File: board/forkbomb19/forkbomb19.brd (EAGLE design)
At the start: 89.2 x 57 mm, 67 parts, among them T3 MMUN2133LT1G, U1 ESP-WROOM-03, U4 TPS61090RSAR, U5 MCP73871, X3 POT_GND, X4 POT_3V3, X5 POT_SIG

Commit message: performing board review
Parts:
- TOUCH: value TOUCHPAD -> TOUCHPADTOUCH_BLANK; device forkbomb19:TOUCHPAD_9.5MM -> forkbomb19:TOUCH_BLANK
- moved LOGO1 147.7 mm to (118.5, 83.1), flipped to the bottom
- moved X3 80.8 mm to (157.1, 77.9)
- moved X5 80.8 mm to (156.8, 71.6)
- moved C14 80.6 mm to (121.3, 63.3)
- moved C9 80.6 mm to (83.6, 80.2)
- moved CHRG 80.6 mm to (88.9, 54.1)
- moved FID1 80.6 mm to (76.8, 35.8)
- moved FID3 80.6 mm to (159.3, 87.0)
- moved FID4 80.6 mm to (75.3, 70.1)
- moved LOGO_G 80.6 mm to (145.7, 39.1)
- moved LOW_BATT 80.6 mm to (91.0, 37.4)
- moved R11 80.6 mm to (150.3, 46.0)
- moved R12 80.6 mm to (85.5, 68.9)
- moved R18 80.6 mm to (80.4, 47.1)
- moved R19 80.6 mm to (85.6, 38.8)
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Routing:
- net TOUCH2: track 74.7 -> 72.1 mm
- net GND: vias 33 -> 34
- net N$23: vias 0 -> 2
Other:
- outline, holes or cut-outs redrawn
- board text added: "Grant Haack"
- board text added: "Open Source Hardware CC-BY-SA-4.0"
- board text added: "ghaack ichorous squar3r00t"

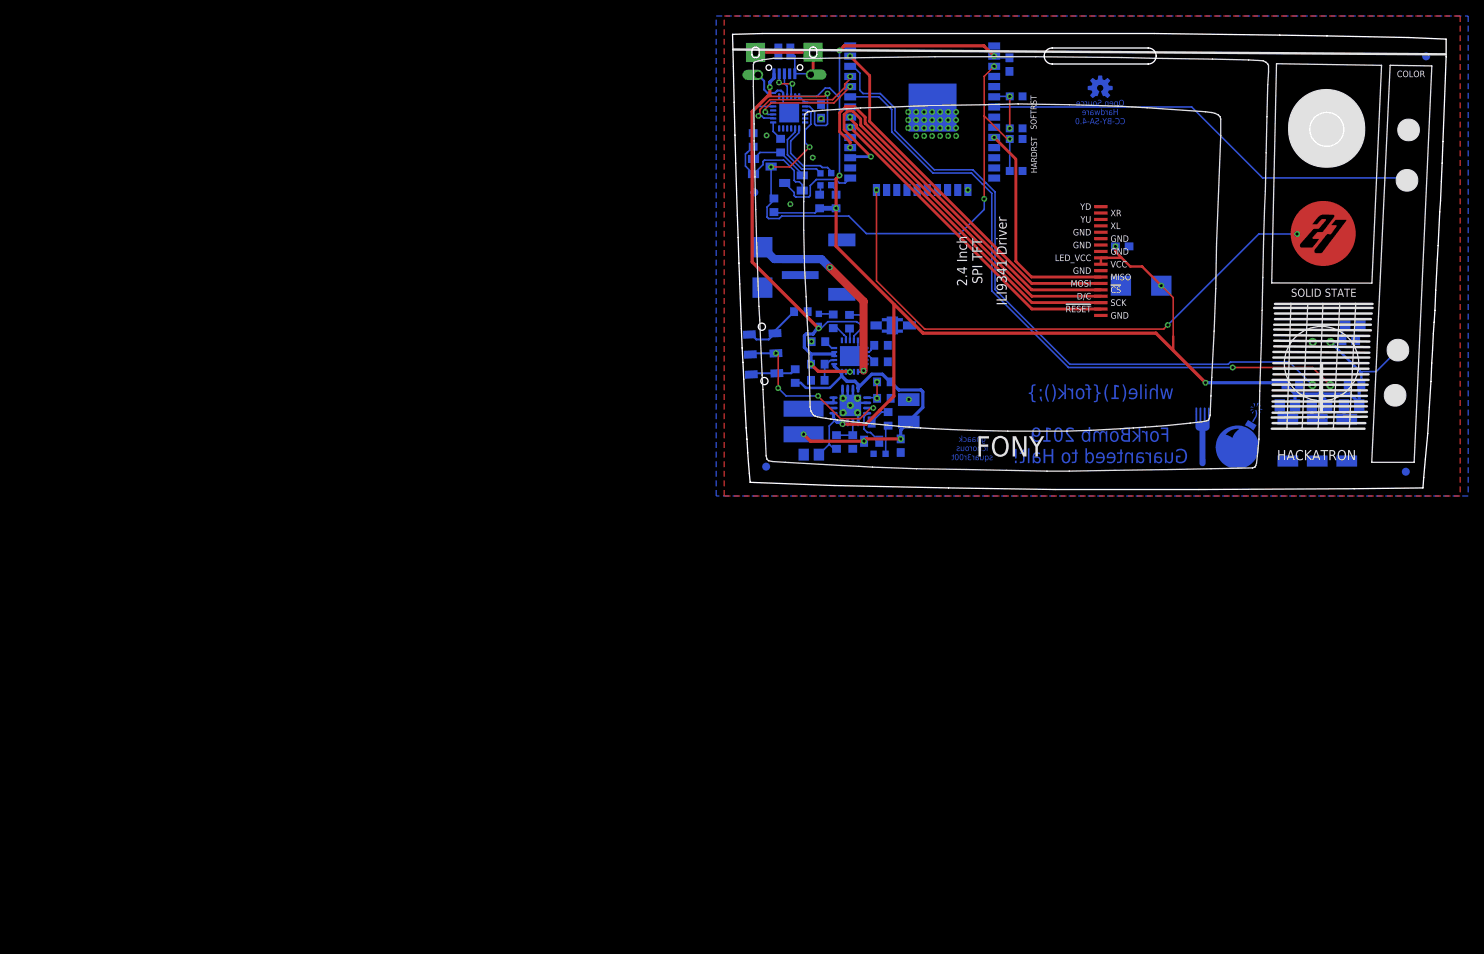
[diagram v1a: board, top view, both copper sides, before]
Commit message: TODO: Add rotary encoder, add another button, pwm the lights
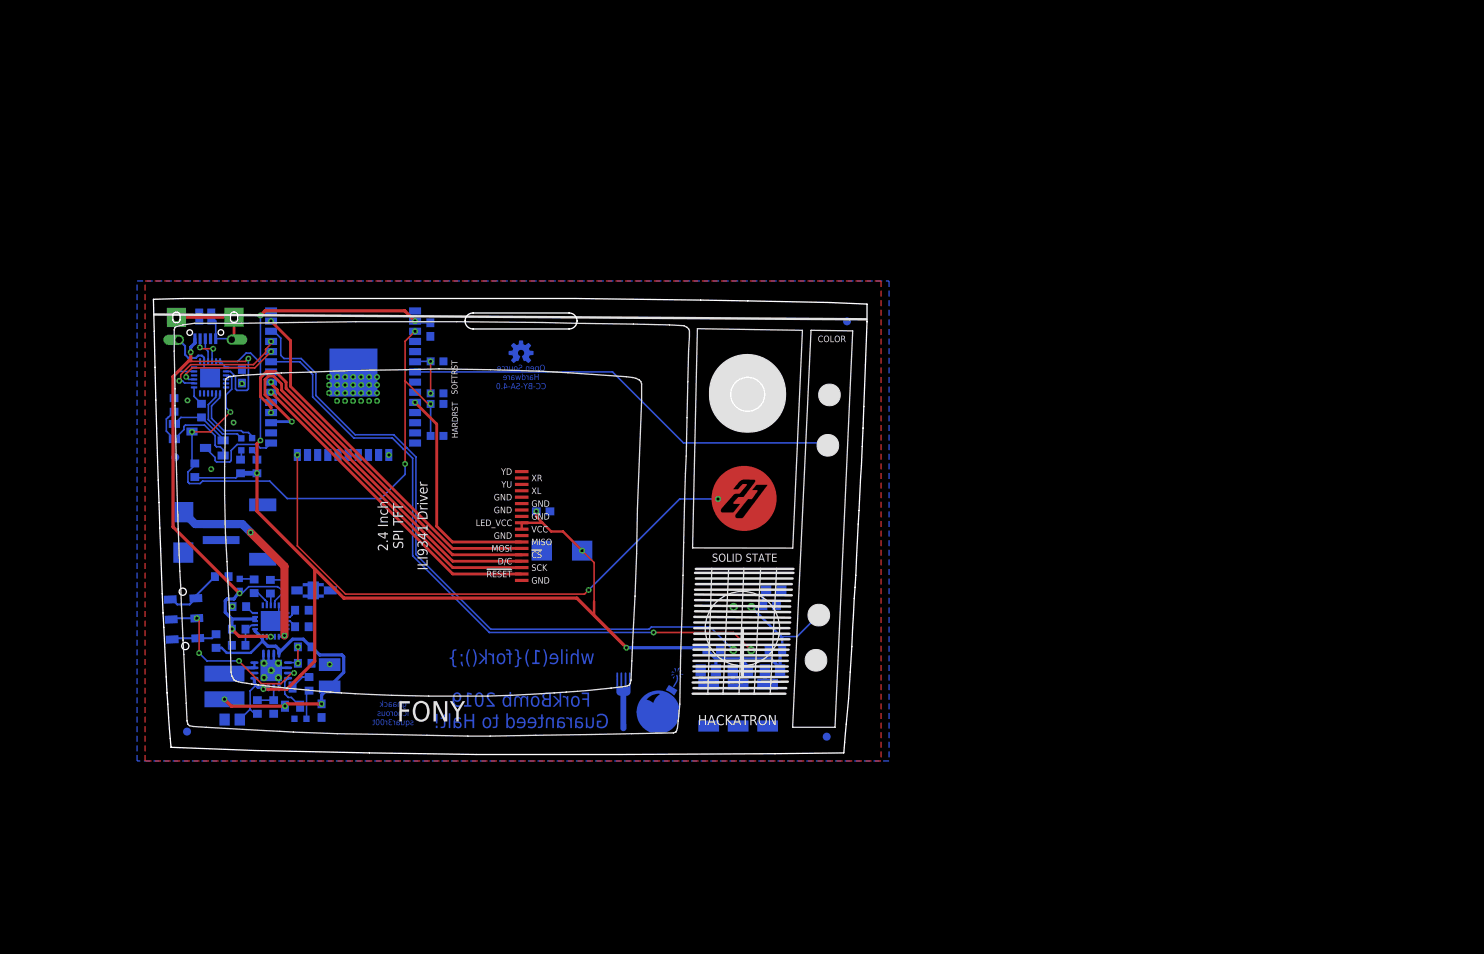
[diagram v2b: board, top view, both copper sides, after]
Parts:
- moved C1 79.6 mm to (34.8, 52.9)
- moved C14 79.6 mm to (48.9, 30.2)
- moved C9 79.6 mm to (11.3, 47.1)
- moved FID3 79.6 mm to (86.9, 53.9)
- moved LOGO_G 79.6 mm to (73.3, 5.94)
- moved R11 79.6 mm to (77.9, 12.9)
- moved R22 79.6 mm to (69.5, 10.3)
- moved R29 79.6 mm to (18.7, 15.8)
- moved R30 79.6 mm to (18.7, 17.8)
- moved R7 79.6 mm to (2.76, 43.5)
- moved U$7 79.6 mm to (73.8, 15.5)
- moved X3 79.6 mm to (84.7, 44.8)
- moved B1 79.6 mm to (12.3, 27.6)
- moved C10 79.6 mm to (3.92, 27.5)
- moved C11 79.6 mm to (77.2, 18.3)
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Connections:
- removed net TSCRN_X1: U1.13
- removed net TSCRN_X2: U1.14
- removed net TSCRN_Y1: U1.11
- removed net TSCRN_Y2: U1.12

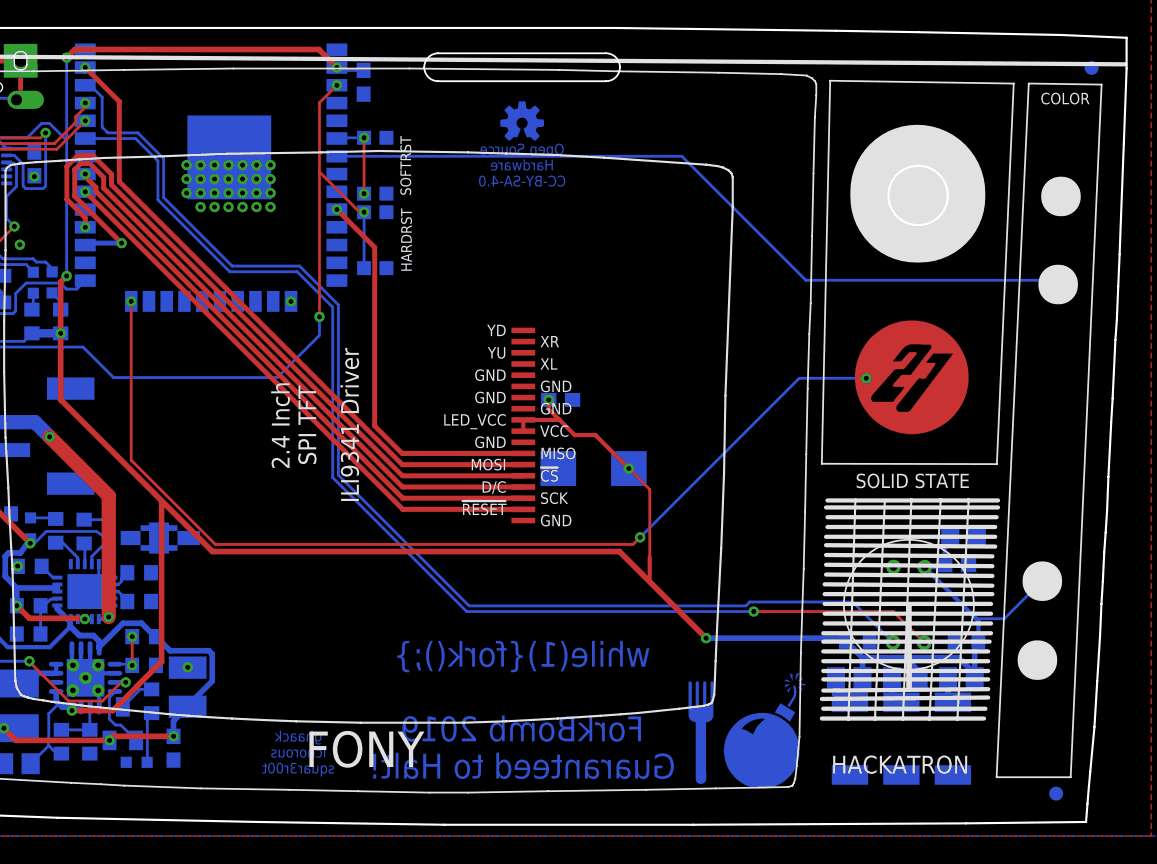
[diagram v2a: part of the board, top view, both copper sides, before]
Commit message: added PWM control for LEDs, swapped the potentiometer for a rotary encoder, and added a menu button
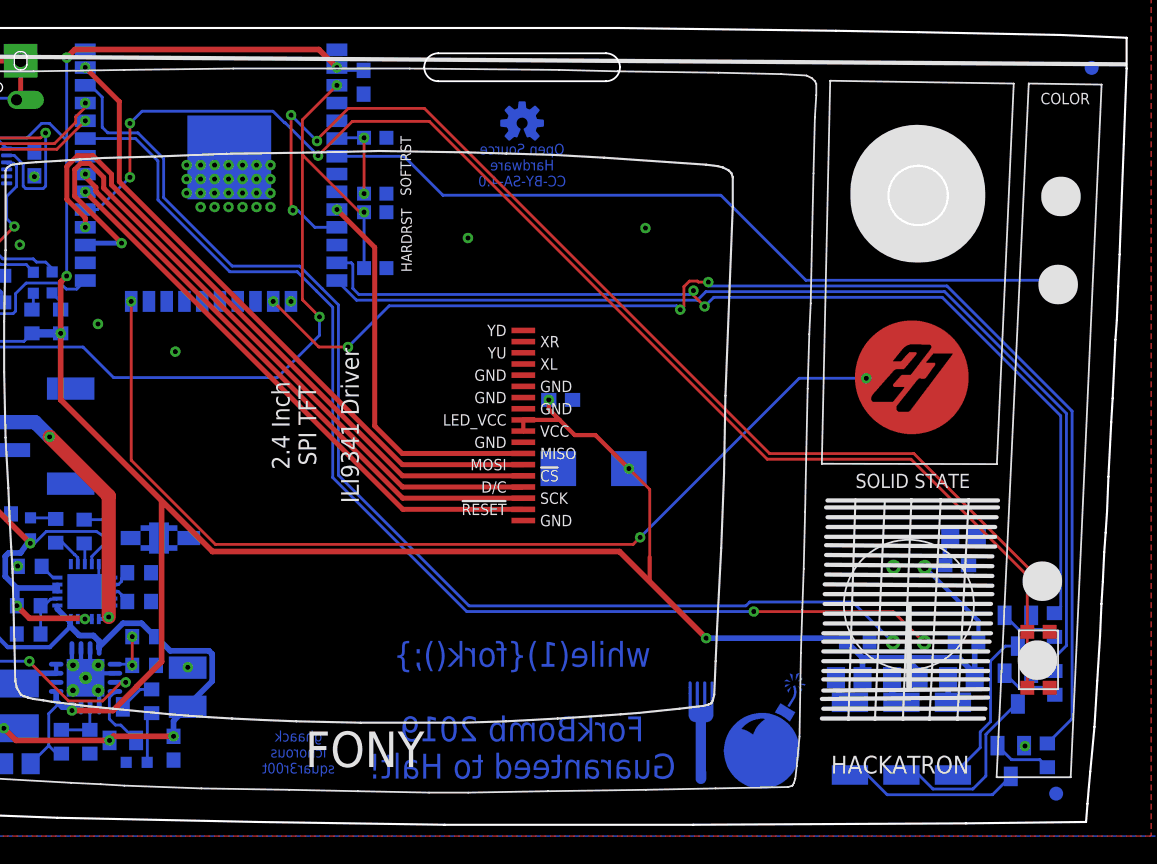
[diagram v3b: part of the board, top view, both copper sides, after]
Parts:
- added MENU: (no value), adafruit:KMR2
- added R13, R4, R5: 1K, rcl:R0603
- added T4, T5, T6: (no value), transistor:SOT23-BEC
- HARDRST, SOFTRESET: value SPST_TACT-KMR2 -> (none)
- renumbered X3 to ROTARY_GND, X4 to ROTARY_B, X5 to ROTARY_A
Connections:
- net N$4 renamed ROTARY_A
- new net BLU_PWM: R13.2, U1.13
- new net GRN_PWM: R5.2, U1.14
- new net MENU: MENU.1, MENU.3, U1.29
- new net N$10: R5.1, T5.B
- new net N$11: R13.1, T6.B
- new net N$14: R4.1, T4.B
- new net N$4: LOGO_B.2, T6.C
- new net N$8: LOGO_G.2, T5.C
- new net N$9: LOGO_R.2, T4.C
- new net RED_PWM: R4.2, U1.16
- new net ROTARY_B: ROTARY_B.1, U1.11
- net +3V3: no longer ROTARY_B.1
- net GND: now also MENU.2, MENU.4, T4.E, T5.E, T6.E; no longer LOGO_B.2, LOGO_G.2, LOGO_R.2
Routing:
- net MENU: track 0.00 -> 96.4 mm, vias 0 -> 3
- net RED_PWM: track 0.00 -> 90.1 mm, vias 0 -> 4
- net ROTARY_B: track 0.00 -> 80.0 mm, vias 0 -> 3
- net GRN_PWM: track 0.00 -> 75.4 mm
- net BLU_PWM: track 0.00 -> 72.6 mm, vias 0 -> 2
- net N$8: track 0.00 -> 13.0 mm
- net N$9: track 0.00 -> 12.6 mm
- net N$4: track 0.00 -> 11.7 mm
- net +3V3: track 225.0 -> 219.2 mm
- net N$10: track 0.00 -> 4.23 mm
- net N$14: track 0.00 -> 4.21 mm
- net N$11: track 0.00 -> 4.21 mm
- net EN: track 74.6 -> 77.3 mm
- net GND: vias 34 -> 39

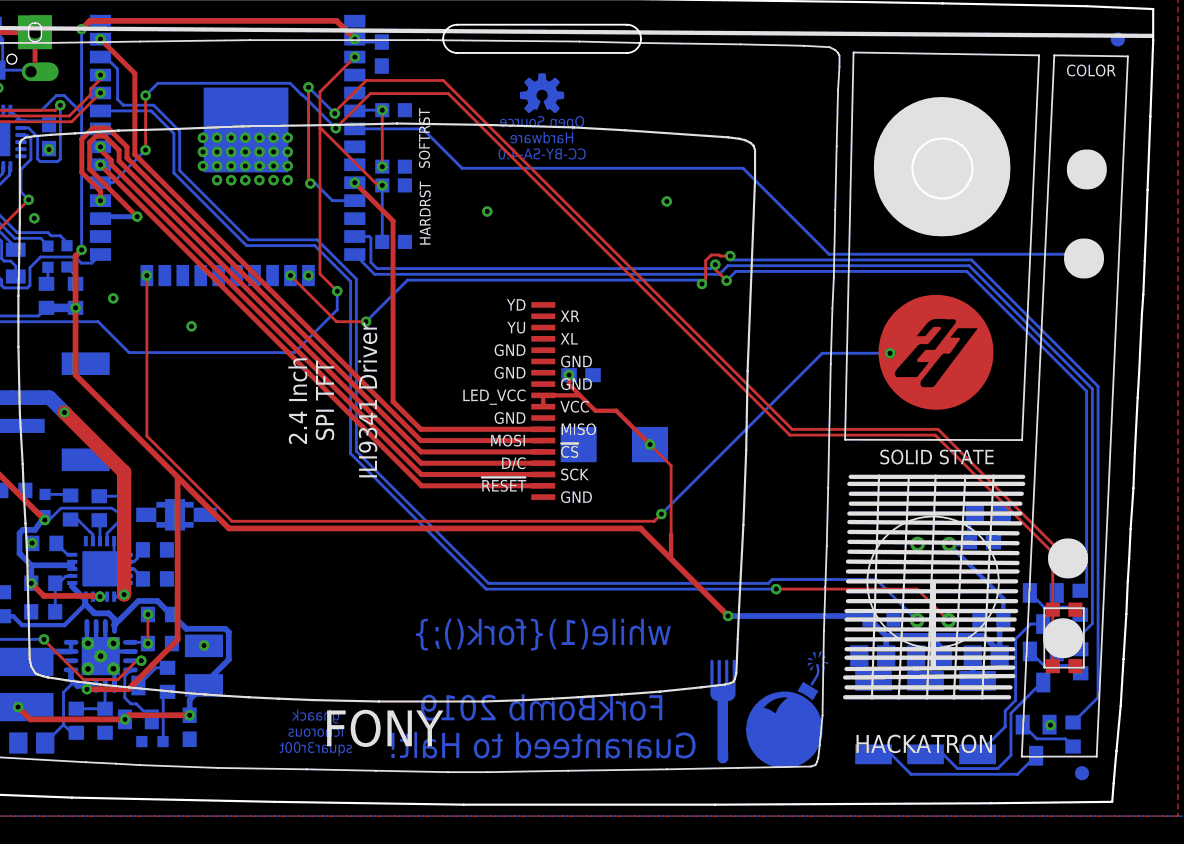
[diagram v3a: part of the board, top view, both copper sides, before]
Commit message: cleaned up board, routed a couple signals
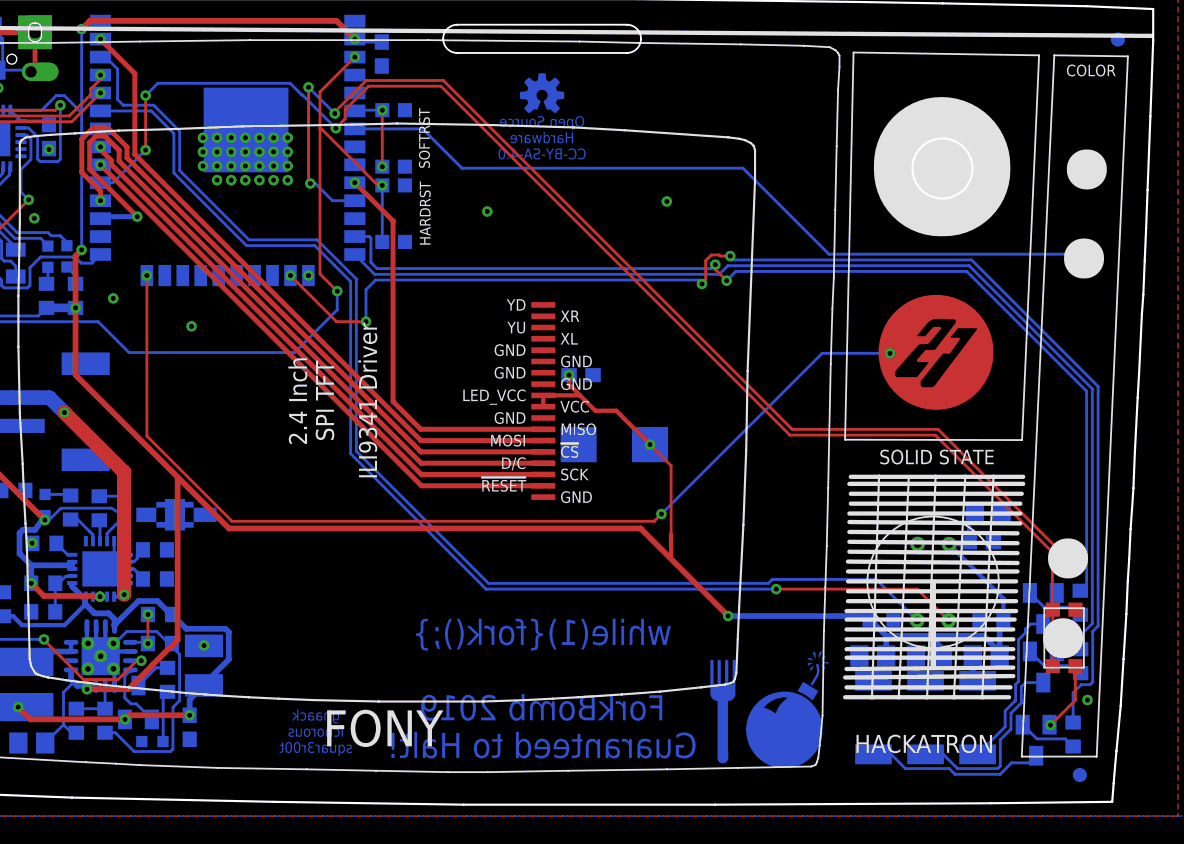
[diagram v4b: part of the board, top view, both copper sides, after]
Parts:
- moved FID2 0.20 mm to (84.2, 1.88)
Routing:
- net GND: track 38.1 -> 62.9 mm, vias 39 -> 41
- net RED_PWM: track 90.1 -> 91.7 mm
- net MENU: track 96.4 -> 97.2 mm
- net N$8: track 13.0 -> 13.7 mm

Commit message: ready for board sign off
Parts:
- added 3V3_ROTARY: POT_GND, con-samtec:TSW-101-XX-G-S
- added C3: 4.7uF, rcl:C0805
- added TP_BATT_GND, TP_BATT_VBAT, TP_BATT_VLIPO, TP_I2C_GND, TP_I2C_SCL, TP_I2C_SDA, TP_PWR_3V3, TP_PWR_GND, TP_PWR_VBUS: TPSTP20SQ, testpad:TP20SQ
- moved ROTARY_A 1.40 mm to (84.6, 39.8)
- moved LOGO1 1.04 mm to (46.0, 51.0)
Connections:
- net TOUCH1 renamed TOUCH0
- new net I2C_GND: TP_I2C_GND.TP
- new net VPP: C3.1, U3.16
- net +3V3: now also 3V3_ROTARY.1, TP_PWR_3V3.TP
- net GND: now also C3.2, TP_BATT_GND.TP, TP_PWR_GND.TP
- net I2C_SCL: now also TP_I2C_SCL.TP
- net I2C_SDA: now also TP_I2C_SDA.TP
- net VBAT: now also TP_BATT_VBAT.TP
- net VBUS: now also TP_PWR_VBUS.TP
- net VLIPO: now also TP_BATT_VLIPO.TP
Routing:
- net +3V3: track 219.2 -> 243.1 mm, vias 8 -> 9
- net VLIPO: track 26.3 -> 39.2 mm
- net VBUS: track 77.3 -> 87.3 mm
- net VPP: track 0.00 -> 6.37 mm, vias 0 -> 2
- net GND: track 62.9 -> 67.7 mm, vias 41 -> 47
- net I2C_SDA: track 85.9 -> 89.3 mm
- net VBAT: track 44.9 -> 47.9 mm
- net I2C_SCL: track 86.3 -> 89.1 mm
- net N$19: track 9.78 -> 8.90 mm
- net N$20: track 8.79 -> 7.99 mm
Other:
- board size 89.2 x 57 mm -> 89.2 x 83.7 mm
- board text added: "+3V3"
- board text added: "+5V"
- board text added: "0xlck 0xkml 0xcwt 0xgph"
- board text added: "CUT HERE JUST FOR FUN"
- board text added: "GND"
- board text added: "ROTARY_3V3"
- board text added: "ROTARY_A"
- board text added: "ROTARY_B"
- board text added: "ROTARY_GND"
- board text added: "SCL"
- board text added: "SDA"
- board text added: "USER"
- board text added: "VBAT"
- board text added: "VLIPO"
- board text removed: "POT_GND"
- board text removed: "SOFTRST"
- board text removed: "ghaack ichorous squar3r00t"

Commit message: working on rev 1.1
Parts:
- removed B1: JST 2-PH, microbuilder:JSTPH2
- removed C10: 100uF, rcl:C/6032-28R
- removed C15: 2.2uF, rcl:C0805
- removed C16: 100nF, rcl:C0603
- removed CHRG: ORANGE, led:CHIP-LED0603
- removed DONE: GREEN, led:CHIP-LED0603
- removed R25: 270K, rcl:R0603
- removed R26, R30: 100K, rcl:R0603
- removed R27, R28: 1K, rcl:R0603
- removed R29: 1.0K, rcl:R0603
- removed THERM: 15K, rcl:R0603
- removed TP_BATT_VLIPO: TPSTP20SQ, testpad:TP20SQ
- removed U5: MCP73871, microbuilder:QFN20_4MM
- added C4: 100uF, resistor:C/6032-28R
- added C5: 100nF, rcl:C0603
- added R14: (no value), rcl:R1210
- added VBAT_GND, VBAT_V: POT_GND, con-samtec:TSW-101-XX-G-S
- R24: value 1.87M -> 1.33M
- moved SOFTRESET 3.53 mm to (39.0, 48.0)
- moved HARDRST 3.39 mm to (39.0, 41.2)
- moved 3V3_ROTARY 0.28 mm to (84.4, 34.9)
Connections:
- removed net N$28: R25.1, R26.1, U5.P$2
- removed net N$29: R28.1, U5.P$7
- removed net N$32: R27.1, U5.P$8
- removed net N$33: R29.2, U5.P$13
- removed net N$34: THERM.2, U5.P$5
- removed net N$35: DONE.C, R28.2
- removed net N$36: CHRG.C, R27.2
- removed net N$37: R30.2, U5.P$12
- removed net N$42: R18.2, U$8.P$1, U$8.P$4
- removed net VLIPO: B1.2, C10.+, TP_BATT_VLIPO.TP, U5.P$14, U5.P$15, U5.P$16
- new net N$15: R7.1, T2.B
- new net N$17: R6.1, T1.B
- net +3V3: now also C4.+, C5.1, R14.2; no longer C15.1, U$2.P$10
- net DAT_TERM_RDY: now also T1.E
- net GND: now also C4.-, C5.2, VBAT_GND.1; no longer B1.1, C10.-, C15.2, C16.2, R26.2, R29.1, R30.1, THERM.1, U5.P$10, U5.P$11, U5.P$21
- net N$1: now also R14.1, U$2.P$10; no longer R7.1, T1.E, T2.B
- net N$13: now also U$8.P$1, U$8.P$4; no longer U$8.P$3, U$8.P$6
- net N$3: now also R18.2, U$8.P$3, U$8.P$6; no longer R6.1, T1.B, T2.E
- net RDY_2_SND: now also T2.E
- net VBAT: now also VBAT_V.1; no longer C16.1, U5.P$1, U5.P$20
- net VBUS: no longer CHRG.A, DONE.A, R25.2, U5.P$17, U5.P$18, U5.P$19, U5.P$3, U5.P$4, U5.P$9
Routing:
- net VLIPO: track 39.2 -> 0.00 mm, vias 2 -> 0
- net VBUS: track 87.3 -> 60.7 mm, vias 5 -> 3
- net N$1: track 14.0 -> 0.00 mm
- net EN: track 77.3 -> 67.3 mm, vias 5 -> 4
- net ENABLE: track 22.5 -> 13.4 mm, vias 4 -> 2
- net DAT_TERM_RDY: track 5.59 -> 13.7 mm
- net N$3: track 7.71 -> 0.00 mm
- net GND: track 67.7 -> 61.1 mm, vias 47 -> 40
- net N$2: track 5.97 -> 0.08 mm, vias 2 -> 0
- net N$42: track 5.76 -> 0.00 mm
- net +3V3: track 243.1 -> 237.7 mm
- net VBAT: track 47.9 -> 42.6 mm, vias 3 -> 2
- net N$15: track 0.00 -> 4.28 mm
- net N$13: track 7.48 -> 3.38 mm
- net N$17: track 0.00 -> 3.99 mm
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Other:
- outline, holes or cut-outs redrawn
- board text added: "Rev 1.1 Maybe it will work this time?"
